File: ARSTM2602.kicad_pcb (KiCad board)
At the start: 2 copper layers, 100 x 100 mm, 99 parts, among them J1 Conn_01x02_Socket, J10 Conn_01x02_Socket, J11 Conn_01x02_Socket, J12 Conn_01x02_Socket, J13 Conn_01x02_Socket, J14 Conn_01x02_Socket, J15 Conn_01x02_Socket, J2 Conn_01x02_Socket, J3 USB_C_Receptacle_USB2.0_14P, J4 USB_C_Receptacle_USB2.0_14P, J8 Conn_01x02_Socket, J9 Conn_ST_STDC14, Q2 Q_NMOS_GSD, Q5 Q_NMOS_GSD, Q6 Q_NMOS_GSD, SW1 SW_Push, SW2 SW_SPDT, SW3 SW_Push, SW4 SW_Push, SW5 SW_Wuerth_450301014042, SW6 SW_Wuerth_450301014042, SW7 SW_Push, SW8 SW_Push, U1 STM32G431RBTx, U10 ESP32-C3-WROOM-02, U11 BD33FC0FP, U12 TLP785, U2 TCAN3414DRBR, U3 TCAN3414DRBR, U4 STM32H523CCTx, U5 BD33FC0FP, U6 ESP32-C3-WROOM-02, U7 BD33FC0FP, U8 TLP785, U9 TLP785

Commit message: 完成(電磁弁制御,モーター出力追加済み)
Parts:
- removed the C10 at (188.2, 39.6)
- removed the C11 at (173.1, 25.6)
- removed the C12 at (169.0, 33.0)
- removed the C13 at (167.5, 33.0)
- removed the C14 at (27.8, 14.3)
- removed the C19 at (194.5, 124.6)
- removed the C20 at (193.0, 124.6)
- removed the C21 at (183.1, 124.7)
- removed the C22 at (181.6, 124.7)
- removed C29, C32: 0.1uF, Capacitor_SMD:C_0603_1608Metric_Pad1.08x0.95mm_HandSolder
- removed C30: 0.1uf, Capacitor_SMD:C_0603_1608Metric_Pad1.08x0.95mm_HandSolder
- removed C31, C33: 1uf, Capacitor_SMD:C_0603_1608Metric_Pad1.08x0.95mm_HandSolder
- removed the D3 at (176.2, 49.5)
- removed the J11 at (212.4, 120.4)
- removed the J14 at (12.4, 4.42)
- removed J15: Conn_01x02_Socket, Connector_JST:JST_XH_S2B-XH-A-1_1x02_P2.50mm_Horizontal
- removed the J9 at (186.0, 23.8)
- removed Q6: Q_NMOS_GSD, Package_TO_SOT_SMD:SOT-23_Handsoldering
- removed the R11 at (177.4, 123.7)
- removed the R5 at (176.1, 25.6)
- removed the R7 at (176.2, 49.5)
- removed the R8 at (202.1, 125.6)
- removed the SW3 at (161.2, 37.4)
- removed the SW6 at (176.8, 120.5)
- removed the U2 at (197.2, 125.1)
- removed the U3 at (180.1, 124.2)
- removed the U4 at (176.2, 33.1)
- removed U8: TLP785, Package_DIP:DIP-4_W7.62mm
- added C1: 1uf, Capacitor_SMD:C_0603_1608Metric_Pad1.08x0.95mm_HandSolder, B.Cu at (97.1, 84.5)
- added C17: 0.1uF, Capacitor_SMD:C_0603_1608Metric_Pad1.08x0.95mm_HandSolder, B.Cu at (68.9, 124.6)
- added C2: 0.1uF, Capacitor_SMD:C_0603_1608Metric_Pad1.08x0.95mm_HandSolder, B.Cu at (87.8, 78.2)
- added C25: 22μF, Capacitor_SMD:C_0805_2012Metric_Pad1.18x1.45mm_HandSolder, B.Cu at (111.0, 52.6)
- added C26: 22μF, Capacitor_SMD:C_0805_2012Metric_Pad1.18x1.45mm_HandSolder, B.Cu at (147.4, 76.2)
- added C3: 0.1uF, Capacitor_SMD:C_0603_1608Metric_Pad1.08x0.95mm_HandSolder, B.Cu at (91.3, 84.0)
- added C4: 0.1uF, Capacitor_SMD:C_0603_1608Metric_Pad1.08x0.95mm_HandSolder, B.Cu at (99.1, 84.5)
- added D4: D, Diode_SMD:D_SOD-323F, B.Cu at (130.8, 140.1)
- added D5: D, Diode_SMD:D_SOD-323F, B.Cu at (120.0, 139.5)
- added D6: D, Diode_SMD:D_SOD-323F, B.Cu at (109.2, 140.0)
- added D7: D, Diode_SMD:D_SOD-323F, B.Cu at (99.1, 140.0)
- added D8: D, Diode_SMD:D_SOD-323F, B.Cu at (88.9, 139.8)
- added G***: LOGO, LOGO, B.Cu at (103.8, 106.1)
- added J1: Conn_01x03_Pin, Connector_JST:JST_XH_S3B-XH-A-1_1x03_P2.50mm_Horizontal, F.Cu at (72.8, 57.6)
- added J17: Conn_01x02_Socket, Connector_JST:JST_XH_S2B-XH-A-1_1x02_P2.50mm_Horizontal, F.Cu at (129.4, 142.3)
- added J18: Conn_01x02_Socket, Connector_JST:JST_XH_S2B-XH-A-1_1x02_P2.50mm_Horizontal, F.Cu at (118.6, 142.3)
- added J19: Conn_01x02_Socket, Connector_JST:JST_XH_S2B-XH-A-1_1x02_P2.50mm_Horizontal, F.Cu at (107.8, 142.3)
- added J20: Conn_01x02_Socket, Connector_JST:JST_XH_S2B-XH-A-1_1x02_P2.50mm_Horizontal, F.Cu at (97.7, 142.3)
- added J21: Conn_01x02_Socket, Connector_JST:JST_XH_S2B-XH-A-1_1x02_P2.50mm_Horizontal, F.Cu at (87.5, 142.2)
- added J3: Conn_01x03_Pin, Connector_JST:JST_XH_S3B-XH-A-1_1x03_P2.50mm_Horizontal, F.Cu at (57.6, 74.7)
- added J4: Conn_01x03_Pin, Connector_JST:JST_XH_S3B-XH-A-1_1x03_P2.50mm_Horizontal, F.Cu at (57.6, 86.6)
- added J5: Conn_01x03_Pin, Connector_JST:JST_XH_S3B-XH-A-1_1x03_P2.50mm_Horizontal, F.Cu at (57.6, 97.6)
- added J6: Conn_01x03_Pin, Connector_JST:JST_XH_S3B-XH-A-1_1x03_P2.50mm_Horizontal, F.Cu at (57.6, 109.5)
- added J7: Conn_01x03_Pin, Connector_JST:JST_XH_S3B-XH-A-1_1x03_P2.50mm_Horizontal, F.Cu at (57.6, 121.5)
- added JP1: Jumper_3_Bridged12, Connector_PinHeader_2.54mm:PinHeader_1x03_P2.54mm_Vertical, F.Cu at (135.7, 62.7)
- added JP2: Jumper_3_Bridged12, Connector_PinHeader_2.54mm:PinHeader_1x03_P2.54mm_Vertical, F.Cu at (134.0, 100.2)
- added Q1: Q_NMOS_GSD, Package_TO_SOT_SMD:SOT-23_Handsoldering, F.Cu at (130.4, 135.1)
- added Q3: Q_NMOS_GSD, Package_TO_SOT_SMD:SOT-23_Handsoldering, F.Cu at (108.8, 135.1)
- added Q4: Q_NMOS_GSD, Package_TO_SOT_SMD:SOT-23_Handsoldering, F.Cu at (98.7, 135.1)
- added R13: 330, Resistor_SMD:R_0603_1608Metric_Pad0.98x0.95mm_HandSolder, B.Cu at (132.8, 130.4)
- added R14: 10k, Resistor_SMD:R_0805_2012Metric, B.Cu at (128.8, 129.7)
- added R24: 10k, Resistor_SMD:R_0805_2012Metric, B.Cu at (97.0, 135.1)
- added R25: 330, Resistor_SMD:R_0603_1608Metric_Pad0.98x0.95mm_HandSolder, B.Cu at (90.7, 130.4)
- added R26: 10k, Resistor_SMD:R_0805_2012Metric, B.Cu at (86.8, 129.7)
- added R27: 10k, Resistor_SMD:R_0805_2012Metric, B.Cu at (86.8, 135.1)
- added R6: 120, Resistor_SMD:R_0603_1608Metric_Pad0.98x0.95mm_HandSolder, B.Cu at (68.1, 129.3)
- added U10: TLP785, Package_DIP:DIP-4_W7.62mm, F.Cu at (123.7, 131.3)
- added U11: TLP785, Package_DIP:DIP-4_W7.62mm, F.Cu at (113.0, 131.3)
- added U13: TLP785, Package_DIP:DIP-4_W7.62mm, F.Cu at (92.5, 131.3)
- added U5: TCAN3414DRBR, TCAN3414DRBR:XCVR_TCAN3414DRBR, F.Cu at (68.3, 126.1)
- C18: value 0.1uF -> 4.7uF; moved to B.Cu
- C23: value 0.1uF -> 0.1μF; footprint Capacitor_SMD:C_0603_1608Metric_Pad1.08x0.95mm_HandSolder -> Capacitor_SMD:C_0603_1608Metric; moved to B.Cu
- C24: value 4.7uf -> 0.1μF; footprint Capacitor_SMD:C_0805_2012Metric_Pad1.18x1.45mm_HandSolder -> Capacitor_SMD:C_0603_1608Metric; moved to B.Cu
- C5: value 2.2μF -> 0.1uF
- C6: value 2.2μF -> 4.7uf; footprint Capacitor_SMD:C_0603_1608Metric_Pad1.08x0.95mm_HandSolder -> Capacitor_SMD:C_0805_2012Metric_Pad1.18x1.45mm_HandSolder
- C8: value 0.1uF -> 0.1uf
- C9: value 0.1uF -> 1uf
- J10: value Conn_01x02_Socket -> Conn_ST_STDC14; footprint Connector_JST:JST_XH_S2B-XH-A-1_1x02_P2.50mm_Horizontal -> Connector_PinHeader_1.27mm:PinHeader_2x07_P1.27mm_Vertical
- J2: value Conn_01x02_Socket -> Conn_01x03_Pin; footprint Connector_AMASS:AMASS_XT30PW-M_1x02_P2.50mm_Horizontal -> Connector_JST:JST_XH_S3B-XH-A-1_1x03_P2.50mm_Horizontal
- J8: footprint Connector_JST:JST_XH_S2B-XH-A-1_1x02_P2.50mm_Horizontal -> Connector_AMASS:AMASS_XT30PW-M_1x02_P2.50mm_Horizontal
- R10: renamed from R13; footprint Resistor_SMD:R_0603_1608Metric_Pad0.98x0.95mm_HandSolder -> Resistor_SMD:R_0805_2012Metric
- R11: renamed from R14; footprint Resistor_SMD:R_0603_1608Metric_Pad0.98x0.95mm_HandSolder -> Resistor_SMD:R_0805_2012Metric
- R15, R17: value 330 -> 10k; footprint Resistor_SMD:R_0603_1608Metric_Pad0.98x0.95mm_HandSolder -> Resistor_SMD:R_0805_2012Metric; moved to B.Cu
- R16, R22: value 10k -> 330; moved to B.Cu
- R18, R20, R21, R23: footprint Resistor_SMD:R_0603_1608Metric_Pad0.98x0.95mm_HandSolder -> Resistor_SMD:R_0805_2012Metric; moved to B.Cu
- R19: moved to B.Cu
- R3: renamed from R6; footprint Resistor_SMD:R_0603_1608Metric_Pad0.98x0.95mm_HandSolder -> Resistor_SMD:R_0805_2012Metric
- R4: renamed from R3; footprint Resistor_SMD:R_0603_1608Metric_Pad0.98x0.95mm_HandSolder -> Resistor_SMD:R_0805_2012Metric
- R5: renamed from R4; footprint Resistor_SMD:R_0603_1608Metric_Pad0.98x0.95mm_HandSolder -> Resistor_SMD:R_0805_2012Metric
- R9: renamed from R12; footprint Resistor_SMD:R_0603_1608Metric_Pad0.98x0.95mm_HandSolder -> Resistor_SMD:R_0805_2012Metric
- SW2: value SW_SPDT -> SW_Push; footprint Button_Switch_THT:SW_Slide-03_Wuerth-WS-SLTV_10x2.5x6.4_P2.54mm -> Button_Switch_SMD:SW_Push_SPST_NO_Alps_SKRK
- SW3: renamed from SW1; footprint Button_Switch_THT:SW_PUSH_6mm -> Button_Switch_SMD:SW_Push_SPST_NO_Alps_SKRK
- SW4: footprint Button_Switch_THT:SW_PUSH_6mm -> Button_Switch_SMD:SW_Push_SPST_NO_Alps_SKRK
- SW5: value SW_Wuerth_450301014042 -> SW_DPDT_x2
- SW6: renamed from SW7; footprint Button_Switch_THT:SW_PUSH_6mm -> Button_Switch_SMD:SW_Push_SPST_NO_Alps_SKRK
- SW7: renamed from SW8; footprint Button_Switch_THT:SW_PUSH_6mm -> Button_Switch_SMD:SW_Push_SPST_NO_Alps_SKRK
- moved C13 176.8 mm to (97.1, 51.6)
- moved SW3 174.1 mm to (95.7, 53.8), turned to 0 degrees
- moved U9 172.6 mm to (134.4, 131.3), turned to 180 degrees
- moved R3 168.0 mm to (108.0, 51.8), turned to 90 degrees
- moved U7 165.0 mm to (125.9, 89.0), turned to 180 degrees
- moved C20 161.9 mm to (130.4, 91.2), turned to 180 degrees
- moved SW4 160.5 mm to (101.9, 53.8), turned to 0 degrees
- moved D3 158.1 mm to (131.0, 89.0), turned to 180 degrees
- moved C21 157.1 mm to (130.2, 86.6), turned to 180 degrees
- moved R5 156.0 mm to (110.9, 59.8), turned to 0 degrees
- moved C22 155.6 mm to (131.4, 82.6), turned to 180 degrees
- moved C19 154.2 mm to (145.8, 63.9)
- moved U3 153.0 mm to (118.5, 56.8), turned to 0 degrees
- moved R4 150.8 mm to (126.0, 53.8), turned to 180 degrees
- moved R15 150.8 mm to (128.8, 135.1), turned to -90 degrees
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- renumbered C15 to C10, C16 to C11, C17 to C12, C1 to C13, C25 to C14, C26 to C15, C2 to C16, C3 to C19, C27 to C20, C28 to C21, C4 to C22, D4 to D1, D6 to D2, D7 to D3, H3 to H2, H2 to H3, J3 to J11, J4 to J14, J1 to J9, R9 to R7, R10 to R8, U5 to U2, U6 to U3, U7 to U4, U10 to U6, U11 to U7
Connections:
- net /Si_3 renamed /Si3
- C10 pad 1: +24V -> +7.5V
- C14 pad 1: +5V -> Net-(D2-K)
- C18 pad 1: +3.3V -> GND
- C18 pad 2: GND -> +3.3V
- C20 pad 1: +5V -> Net-(D3-K)
- C23 pad 1: +3.3V -> +3V3
- C24 pad 1: +3.3V -> +3V3
- C5 pad 1: GND -> +3.3V
- C5 pad 2: Net-(C5-Pad2) -> GND
- C6 pad 1: GND -> +3.3V
- C6 pad 2: Net-(C6-Pad2) -> GND
- C8 pad 1: +3.3V -> GND
- C8 pad 2: GND -> +3.3V
- C9 pad 1: +3.3V -> GND
- C9 pad 2: GND -> +3.3V
- D1 pad 1: +24V -> +7.5V
- D2 pad 1: +5V -> Net-(D2-K)
- D3 pad 1: +5V -> Net-(D3-K)
- J10 pad 1: +24V -> unconnected-(J10-NC-Pad1)
- J10 pad 2: Net-(D5-A) -> unconnected-(J10-NC-Pad2)
- J11 pad A6: esp_d+ -> /ESP/esp_d+
- J11 pad A7: esp_d- -> /ESP/esp_d-
- J11 pad B6: esp_d+ -> /ESP/esp_d+
- J11 pad B7: esp_d- -> /ESP/esp_d-
- J12 pad 1: CAN1_+ -> /can1/can-
- J12 pad 2: CAN1_- -> /can1/can+
- J13 pad 1: CAN1_- -> /can1/can-
- J13 pad 2: CAN1_+ -> /can1/can+
- J14 pad A6: esp_d+ -> /ESP1/esp_d+
- J14 pad A7: esp_d- -> /ESP1/esp_d-
- J14 pad B6: esp_d+ -> /ESP1/esp_d+
- J14 pad B7: esp_d- -> /ESP1/esp_d-
- J2 pad 1: +24V -> GND
- J2 pad 2: GND1 -> Tim1ch3
- J8 pad 1: CAN2_+ -> GND1
- J8 pad 2: CAN2_- -> +24V
- J9 pad 2: +24V -> +7.5V
- R15 pad 2: /Si_1 -> GND1
- R16 pad 2: Net-(Q2-G) -> /Si2
- R17 pad 2: /Si_2 -> Net-(Q2-G)
- R18 pad 1: Net-(R18-Pad1) -> Net-(Q2-G)
- R18 pad 2: Net-(Q5-G) -> GND1
- R20 pad 2: Net-(Q6-G) -> Net-(Q3-G)
- R21 pad 1: Net-(Q5-G) -> Net-(Q3-G)
- R22 pad 1: Net-(Q2-G) -> Net-(R22-Pad1)
- R22 pad 2: GND1 -> /Si4
- R23 pad 1: Net-(Q6-G) -> Net-(R23-Pad1)
- R23 pad 2: GND1 -> Net-(Q4-G)
- SW2 pad 1: GND -> nrst
- SW2 pad 2: BOOT0 -> GND
- SW5 pad 1: CAN2_- -> /can1/canR
- SW5 pad 2: unconnected-(SW5-C-Pad2) -> /can1/can-
- SW5 pad 3: CAN2R -> unconnected-(SW5A-C-Pad3)
- U1 pad 10: unconnected-(U1-PC2-Pad10) -> Tim1ch3
- U1 pad 11: unconnected-(U1-PC3-Pad11) -> dir2
- U1 pad 12: unconnected-(U1-PA0-Pad12) -> Tim2ch1
- U1 pad 13: unconnected-(U1-PA1-Pad13) -> dir3
- U1 pad 14: unconnected-(U1-PA2-Pad14) -> Tim2ch3
- U1 pad 17: unconnected-(U1-PA3-Pad17) -> dir4
- U1 pad 18: unconnected-(U1-PA4-Pad18) -> Tim3ch2
- U1 pad 19: unconnected-(U1-PA5-Pad19) -> dir5
- U1 pad 20: unconnected-(U1-PA6-Pad20) -> Tim3ch1
- U1 pad 21: unconnected-(U1-PA7-Pad21) -> dir6
- U1 pad 24: unconnected-(U1-PB0-Pad24) -> Tim3ch3
- U1 pad 25: unconnected-(U1-PB1-Pad25) -> dir7
- U1 pad 34: unconnected-(U1-PB12-Pad34) -> /spi_cs_2
- U1 pad 35: unconnected-(U1-PB13-Pad35) -> /spi_sclk_2
- U1 pad 36: unconnected-(U1-PB14-Pad36) -> /spi_miso_2
- U1 pad 37: unconnected-(U1-PB15-Pad37) -> /spi_mosi_2
- U1 pad 38: unconnected-(U1-PC6-Pad38) -> /spi_int_2
- U1 pad 49: unconnected-(U1-PA13-Pad49) -> swdio
- U1 pad 50: unconnected-(U1-PA14-Pad50) -> swclk
- U1 pad 51: unconnected-(U1-PA15-Pad51) -> /spi_cs_3
- U1 pad 52: unconnected-(U1-PC10-Pad52) -> /spi_sclk_3
- U1 pad 53: unconnected-(U1-PC11-Pad53) -> /spi_miso_3
- U1 pad 54: unconnected-(U1-PC12-Pad54) -> /spi_mosi_3
- U1 pad 55: unconnected-(U1-PD2-Pad55) -> /spi_int_3
- U1 pad 57: unconnected-(U1-PB4-Pad57) -> uart2-rx
- U1 pad 58: unconnected-(U1-PB5-Pad58) -> uart2-tx
- U1 pad 61: unconnected-(U1-PB8-Pad61) -> can1_tx
- U1 pad 62: unconnected-(U1-PB9-Pad62) -> can1_rx
- U1 pad 7: unconnected-(U1-PG10-Pad7) -> nrst
- U1 pad 8: unconnected-(U1-PC0-Pad8) -> Tim1ch1
- U1 pad 9: unconnected-(U1-PC1-Pad9) -> dir1
- U12 pad 1: Net-(R19-Pad1) -> Net-(R22-Pad1)
- U12 pad 3: Net-(R20-Pad1) -> Net-(R23-Pad1)
- U2 pad 1: +24V -> +7.5V
- U3 pad 13: esp_d- -> /ESP/esp_d-
- U3 pad 14: esp_d+ -> /ESP/esp_d+
- U3 pad 15: unconnected-(U6-IO3-Pad15) -> /spi_int_3
- U3 pad 3: /sda -> /spi_mosi_3
- U3 pad 4: /scl -> /spi_miso_3
- U3 pad 5: unconnected-(U6-IO6-Pad5) -> /spi_sclk_3
- U3 pad 6: unconnected-(U6-IO7-Pad6) -> /spi_cs_3
- U4 pad 1: +5V -> Net-(D2-K)
- U6 pad 13: esp_d- -> /ESP1/esp_d-
- U6 pad 14: esp_d+ -> /ESP1/esp_d+
- U6 pad 15: unconnected-(U10-IO3-Pad15) -> /spi_int_2
- U6 pad 3: /sda -> /spi_mosi_2
- U6 pad 4: /scl -> /spi_miso_2
- U6 pad 5: unconnected-(U10-IO6-Pad5) -> /spi_sclk_2
- U6 pad 6: unconnected-(U10-IO7-Pad6) -> /spi_cs_2
- U7 pad 1: +5V -> Net-(D3-K)
- U9 pad 1: Net-(R17-Pad1) -> Net-(R13-Pad1)
- U9 pad 3: Net-(R18-Pad1) -> Net-(R14-Pad1)
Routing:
- net +24V: track 0.00 -> 247.2 mm
- net +3.3V: track 4.24 -> 136.8 mm, vias 2 -> 9
- net +7.5V: track 0.00 -> 113.7 mm, vias 0 -> 1
- net +3V3: track 0.00 -> 104.0 mm, vias 0 -> 8
- net GND1: track 0.00 -> 64.1 mm, vias 0 -> 5
- net GND: track 0.00 -> 62.5 mm, vias 0 -> 76
- net can1_rx: track 0.00 -> 59.9 mm, vias 0 -> 2
- net can1_tx: track 0.00 -> 59.8 mm, vias 0 -> 2
- net dir7: track 0.00 -> 55.4 mm
- net Tim3ch3: track 0.00 -> 53.7 mm
- net /spi_mosi_2: track 0.00 -> 49.9 mm
- net /spi_int_2: track 0.00 -> 49.1 mm, vias 0 -> 2
- net dir6: track 0.00 -> 48.7 mm
- net /spi_miso_2: track 0.00 -> 48.3 mm
- net Tim3ch1: track 0.00 -> 46.9 mm
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- added copper zone on B.Cu, net GND
- added copper zone on F.Cu, net GND

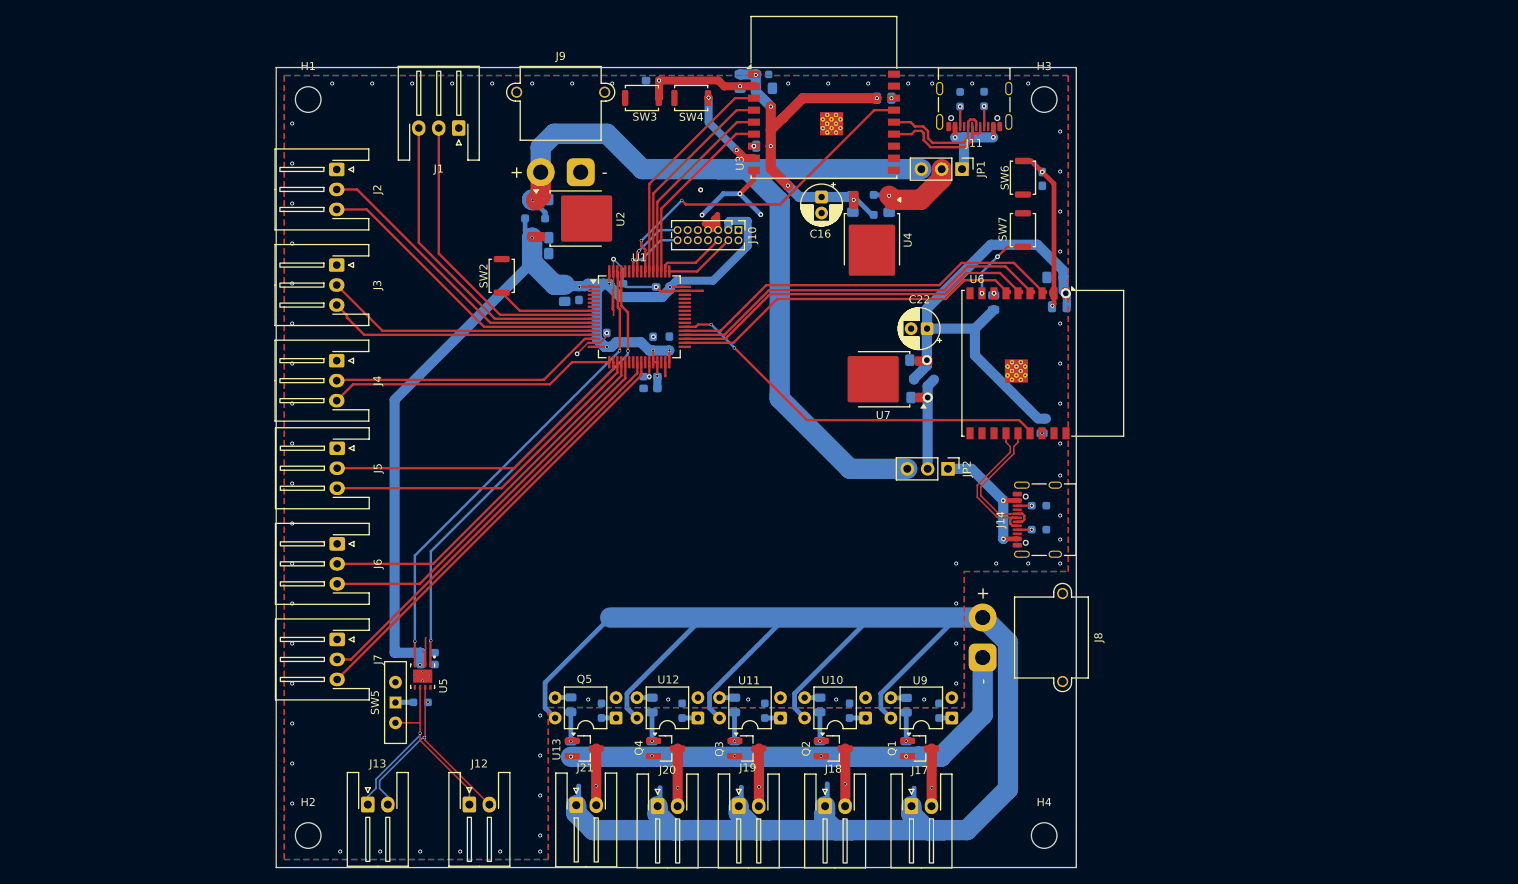
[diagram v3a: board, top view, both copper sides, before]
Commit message: サーボときんていをつけ忘れていたので回路図に追加(部品配置に悩んでる
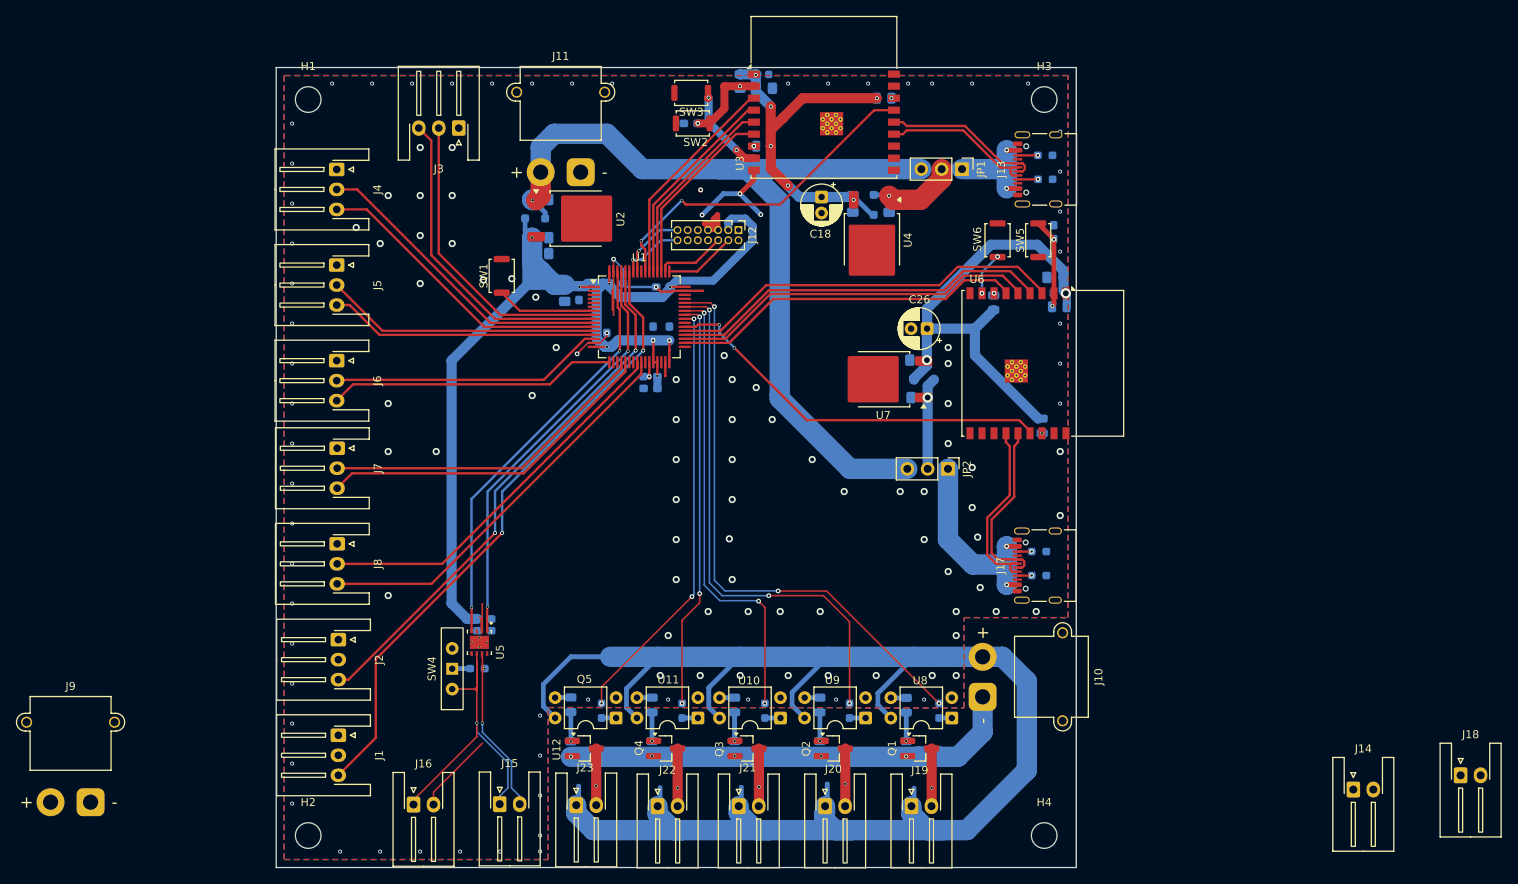
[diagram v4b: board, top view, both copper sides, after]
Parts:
- removed the J7 at (57.6, 121.5)
- added J1: Conn_01x03_Pin, Connector_JST:JST_XH_S3B-XH-A-1_1x03_P2.50mm_Horizontal, F.Cu at (57.8, 133.5)
- added J14: Conn_01x02_Socket, Connector_JST:JST_XH_S2B-XH-A-1_1x02_P2.50mm_Horizontal, F.Cu at (184.6, 140.3)
- added J18: Conn_01x02_Socket, Connector_JST:JST_XH_S2B-XH-A-1_1x02_P2.50mm_Horizontal, F.Cu at (198.1, 138.5)
- added J2: Conn_01x03_Pin, Connector_JST:JST_XH_S3B-XH-A-1_1x03_P2.50mm_Horizontal, F.Cu at (57.8, 121.5)
- added J9: Conn_01x02_Socket, Connector_AMASS:AMASS_XT30PW-M_1x02_P2.50mm_Horizontal, F.Cu at (26.8, 141.8)
- moved R2 12.7 mm to (146.1, 61.0), turned to 0 degrees
- moved R1 12.6 mm to (146.1, 64.0), turned to 0 degrees
- moved J13 11.2 mm to (145.2, 62.7), turned to 90 degrees
- moved C19 8.25 mm to (76.0, 120.4)
- moved C20 8.25 mm to (76.0, 118.9)
- moved U5 8.25 mm to (75.4, 121.8)
- moved R6 8.25 mm to (75.2, 125.1)
- moved SW4 8.25 mm to (72.0, 125.2)
- moved SW5 8.04 mm to (145.2, 71.6)
- moved C13 7.14 mm to (101.8, 57.0)
- moved SW2 7.10 mm to (102.1, 57.0)
- moved C21 6.81 mm to (147.2, 70.6), turned to 90 degrees
- moved R7 5.74 mm to (145.3, 113.5)
- moved J17 5.74 mm to (145.1, 112.3)
- moved R8 5.74 mm to (145.3, 110.5)
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- renumbered C23 to C14, C25 to C15, C14 to C16, C15 to C17, C16 to C18, C17 to C19, C18 to C20, C19 to C21, C24 to C22, C26 to C23, C20 to C24, C21 to C25, C22 to C26, J8 to J10, J9 to J11, J10 to J12, J11 to J13, J12 to J15, J13 to J16, J14 to J17, J17 to J19, J18 to J20, J19 to J21, J20 to J22, J21 to J23, J1 to J3, J2 to J4, J3 to J5, J4 to J6, J5 to J7, J6 to J8, R13 to R12, R14 to R13, R15 to R14, R16 to R15, R17 to R16, R18 to R17, R19 to R18, R20 to R19, R21 to R20, R22 to R21, R23 to R22, R24 to R23, R25 to R24, R26 to R25, R27 to R26, SW2 to SW1, SW3 to SW2, SW4 to SW3, SW5 to SW4, SW6 to SW5, SW7 to SW6, U11 to U10, U12 to U11, U13 to U12, U9 to U8, U10 to U9
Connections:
- net dir1 renamed Tim1ch2
- net dir2 renamed Tim1ch4
- net dir3 renamed Tim2ch2
- net dir4 renamed Tim2ch4
- J7 pad 3: dir5 -> Tim3ch1
- J8 pad 2: Tim3ch1 -> Tim3ch4
- J8 pad 3: dir6 -> Tim3ch3
- U1 pad 18: Tim3ch2 -> unconnected-(U1-PA4-Pad18)
- U1 pad 19: dir5 -> unconnected-(U1-PA5-Pad19)
- U1 pad 20: Tim3ch1 -> Tim3ch2
- U1 pad 21: dir6 -> Tim3ch1
- U1 pad 24: Tim3ch3 -> Tim3ch4
- U1 pad 25: dir7 -> Tim3ch3
- U1 pad 3: unconnected-(U1-PC14-Pad3) -> /emergency_sw
- U1 pad 40: unconnected-(U1-PC8-Pad40) -> /Si5
- U1 pad 41: unconnected-(U1-PC9-Pad41) -> /Si4
- U1 pad 42: unconnected-(U1-PA8-Pad42) -> /Si3
- U1 pad 43: unconnected-(U1-PA9-Pad43) -> /Si2
- U1 pad 44: unconnected-(U1-PA10-Pad44) -> /Si1
- U1 pad 59: unconnected-(U1-PB6-Pad59) -> /Tim4ch1
- U1 pad 60: unconnected-(U1-PB7-Pad60) -> /Tim4ch2
- U5 pad 10: GND -> (no net)
- U5 pad 11: GND -> (no net)
- U5 pad 12: GND -> (no net)
- U5 pad 13: GND -> (no net)
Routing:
- net /Tim4ch1: track 0.00 -> 79.5 mm, vias 0 -> 2
- net /Si1: track 0.00 -> 72.6 mm, vias 0 -> 3
- net /Tim4ch2: track 0.00 -> 67.7 mm, vias 0 -> 2
- net /Si2: track 0.00 -> 67.1 mm, vias 0 -> 3
- net /Si3: track 0.00 -> 57.3 mm, vias 0 -> 3
- net dir7: track 55.4 -> 0.00 mm
- net /Si5: track 0.00 -> 54.0 mm, vias 0 -> 3
- net /Si4: track 0.00 -> 51.2 mm, vias 0 -> 3
- net Tim3ch4: track 0.00 -> 49.3 mm
- net dir6: track 48.7 -> 0.00 mm
- net dir5: track 42.3 -> 0.00 mm
- net +24V: track 247.2 -> 215.7 mm
- net /can1/can-: track 31.9 -> 42.2 mm
- net Net-(U6-EN): track 20.4 -> 11.2 mm
- net +5V: track 28.8 -> 37.9 mm
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
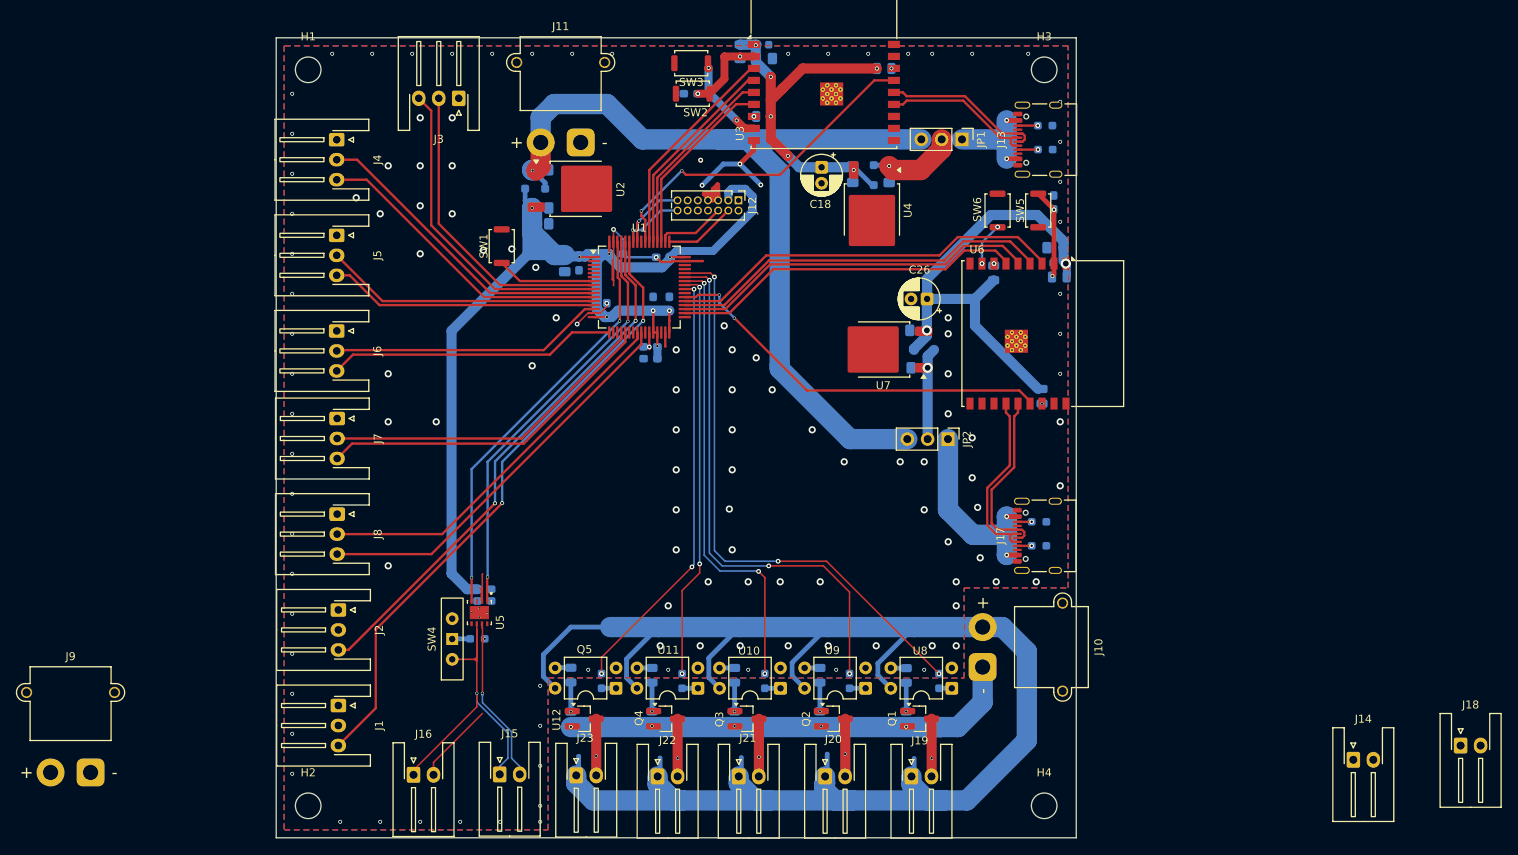
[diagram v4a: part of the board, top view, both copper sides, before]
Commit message: サーボ系ときんてい系の部品の配置と配線
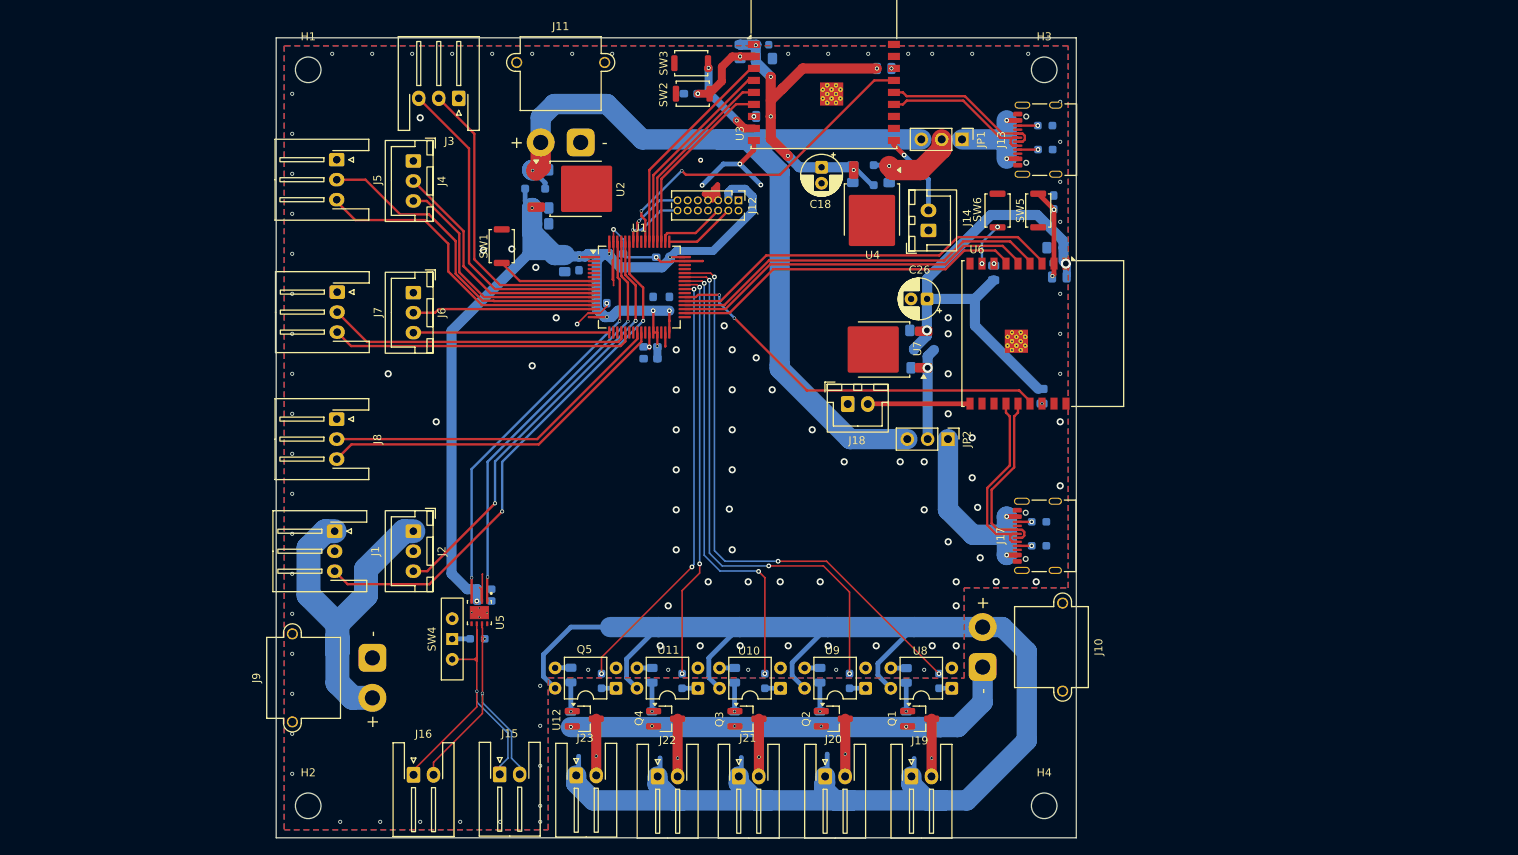
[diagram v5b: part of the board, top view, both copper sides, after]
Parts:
- J14, J18: footprint Connector_JST:JST_XH_S2B-XH-A-1_1x02_P2.50mm_Horizontal -> Connector_JST:JST_XH_B2B-XH-A_1x02_P2.50mm_Vertical
- J2, J4, J6: footprint Connector_JST:JST_XH_S3B-XH-A-1_1x03_P2.50mm_Horizontal -> Connector_JST:JST_XH_B3B-XH-A_1x03_P2.50mm_Vertical
- moved J18 87.7 mm to (121.4, 95.8)
- moved J14 84.8 mm to (131.5, 74.1), turned to 90 degrees
- moved J9 38.0 mm to (62.0, 127.5), turned to 90 degrees
- moved J1 21.8 mm to (57.3, 111.7)
- moved J7 15.8 mm to (57.6, 81.8)
- moved J2 13.6 mm to (67.1, 111.7)
- moved J8 11.9 mm to (57.6, 97.7)
- moved J6 10.7 mm to (67.1, 81.9)
- moved J4 9.94 mm to (67.1, 65.4)
- moved J5 9.45 mm to (57.6, 65.2)
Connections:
- J2 pad 2: unconnected-(J2-Pin_2-Pad2) -> GND
- U3 pad 10: unconnected-(U3-IO10-Pad10) -> /ESP/emergency_sw
- U6 pad 10: unconnected-(U6-IO10-Pad10) -> /ESP1/emergency_sw
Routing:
- net +12V: track 0.00 -> 47.6 mm
- net /Tim4ch2: track 67.7 -> 54.2 mm
- net /ESP1/emergency_sw: track 0.00 -> 13.0 mm
- net /Tim4ch1: track 79.5 -> 67.1 mm
- net Tim2ch4: track 36.1 -> 24.5 mm
- net Tim2ch3: track 34.0 -> 22.8 mm
- net /ESP/emergency_sw: track 0.00 -> 10.5 mm, vias 0 -> 1
- net Tim1ch3: track 39.1 -> 30.9 mm
- net Tim1ch4: track 38.2 -> 30.4 mm
- net Tim2ch1: track 34.5 -> 40.8 mm
- net Tim2ch2: track 33.7 -> 39.8 mm
- net Tim3ch4: track 49.3 -> 43.6 mm
- net Tim3ch1: track 43.2 -> 38.1 mm
- net Tim3ch3: track 50.4 -> 45.3 mm
- net Tim3ch2: track 41.5 -> 38.0 mm
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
